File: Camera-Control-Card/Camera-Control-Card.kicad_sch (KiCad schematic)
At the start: 2 parts, among them J2 Conn_01x10, U3 74AHC125

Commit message: updates
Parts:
- removed U3: 74AHC125, Package_SO:TSSOP-14_4.4x5mm_P0.65mm, symbol 74xx:74AHCT125
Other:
- added sheet Buffer_3V3 (Buffer_3V3.kicad_sch)

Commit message: test
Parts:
- removed J2: Conn_01x10, Connector_PinHeader_2.54mm:PinHeader_2x05_P2.54mm_Vertical, symbol Connector_Generic:Conn_01x10
- added J1, J2, J3, J4, J5: Conn_Coaxial, Connector_Coaxial:SMA_Molex_73251-1153_EdgeMount_Horizontal, symbol Connector:Conn_Coaxial
- added J6: Conn_02x05_Counter_Clockwise, symbol Connector_Generic:Conn_02x05_Counter_Clockwise
- added J8: SFV24R-1STE1HLF, Footprints:AMPHENOL_SFV24R-1STE1HLF, symbol Symbols:SFV24R-1STE1HLF
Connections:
- net +3V3: now also J6.1 (Pin_1)
- net Buffer_3V3/OUT_0: now also J1.1 (In)
- net Buffer_3V3/OUT_1: now also J2.1 (In)
- net Buffer_3V3/OUT_2: now also J3.1 (In)
- net Buffer_3V3/OUT_3: now also J4.1 (In)
- net GND: now also J1.2 (Ext), J2.2 (Ext), J3.2 (Ext), J4.2 (Ext), J5.2 (Ext), J6.4 (Pin_4), J6.5 (Pin_5), J8.10, J8.12, J8.14, J8.16, J8.18, J8.2, J8.20, J8.22, J8.24, J8.4, J8.6, J8.8
- new net Buffer_3V3/OUT_4: J5.1 (In)
- new net DONE: J6.6 (Pin_6)
- new net INIT_N: J6.3 (Pin_3)
- new net PROGRAMN: J6.7 (Pin_7)
- new net TCK: J6.8 (Pin_8)
- new net TDI: J6.10 (Pin_10)
- new net TDO: J6.9 (Pin_9)
- new net TMS: J6.2 (Pin_2)
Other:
- sheet Buffer_3V3 ports: added IN_4, OE_4, OUT_4; removed none

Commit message: Updates
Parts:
- J2: renamed from J6; footprint (none) -> Footprints:AMPHENOL_78207-110HLF
- renumbered J8 to J1, J1 to J3, J2 to J4, J3 to J5, J4 to J6, J5 to J7
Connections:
- net PROGRAMN: now also J2.2 (Pin_2); no longer J2.7 (Pin_7)
- net TCK: now also J2.9 (Pin_9); no longer J2.8 (Pin_8)
- net TDI: now also J2.8 (Pin_8); no longer J2.10 (Pin_10)
- net TDO: now also J2.7 (Pin_7); no longer J2.9 (Pin_9)
- net TMS: now also J2.10 (Pin_10); no longer J2.2 (Pin_2)
- net FPGA/PT35B: now reaches J1.1
- net FPGA/PT28A: now reaches J1.11
- net FPGA/PT25B: now reaches J1.13
- net FPGA/PT25A: now reaches J1.15
- net FPGA/PT22D: now reaches J1.17
- net FPGA/PT22C: now reaches J1.19
- net FPGA/PT18B: now reaches J1.21
- net FPGA/PT18A: now reaches J1.23
- net FPGA/PT35A: now reaches J1.3
- net FPGA/PT33B: now reaches J1.5
- net FPGA/PT33A: now reaches J1.7
- net FPGA/PT28B: now reaches J1.9
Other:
- added sheet USB (USB.kicad_sch)
- sheet FPGA ports: added PT18A, PT18B, PT22C, PT22D, PT25A, PT25B, PT28A, PT28B, PT33A, PT33B, PT35A, PT35B; removed none

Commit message: Camera Control Card layout
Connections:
- net +3V3: now also J2.4 (Pin_4); no longer J2.1 (Pin_1)
- net DONE: now also J2.3 (Pin_3); no longer J2.6 (Pin_6)
- net GND: now also J2.1 (Pin_1), J2.2 (Pin_2); no longer J2.4 (Pin_4), J2.5 (Pin_5)
- net INIT_N: now also J2.6 (Pin_6); no longer J2.3 (Pin_3)
- net PROGRAMN: now also J2.5 (Pin_5); no longer J2.2 (Pin_2)
- no-connect marks 5 -> 2
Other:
- sheet FPGA ports: added MISO_1_BUF, MISO_2_BUF, MOSI_1, MOSI_2, PB26A, PB26B, SCK_1, SCK_2; removed MISO, MOSI, SCK
- sheet USB ports: added +3V3, GND, RXD, TXD; removed none
- moved on the sheet: J1, J2, J3, J4, J5, J6, J7

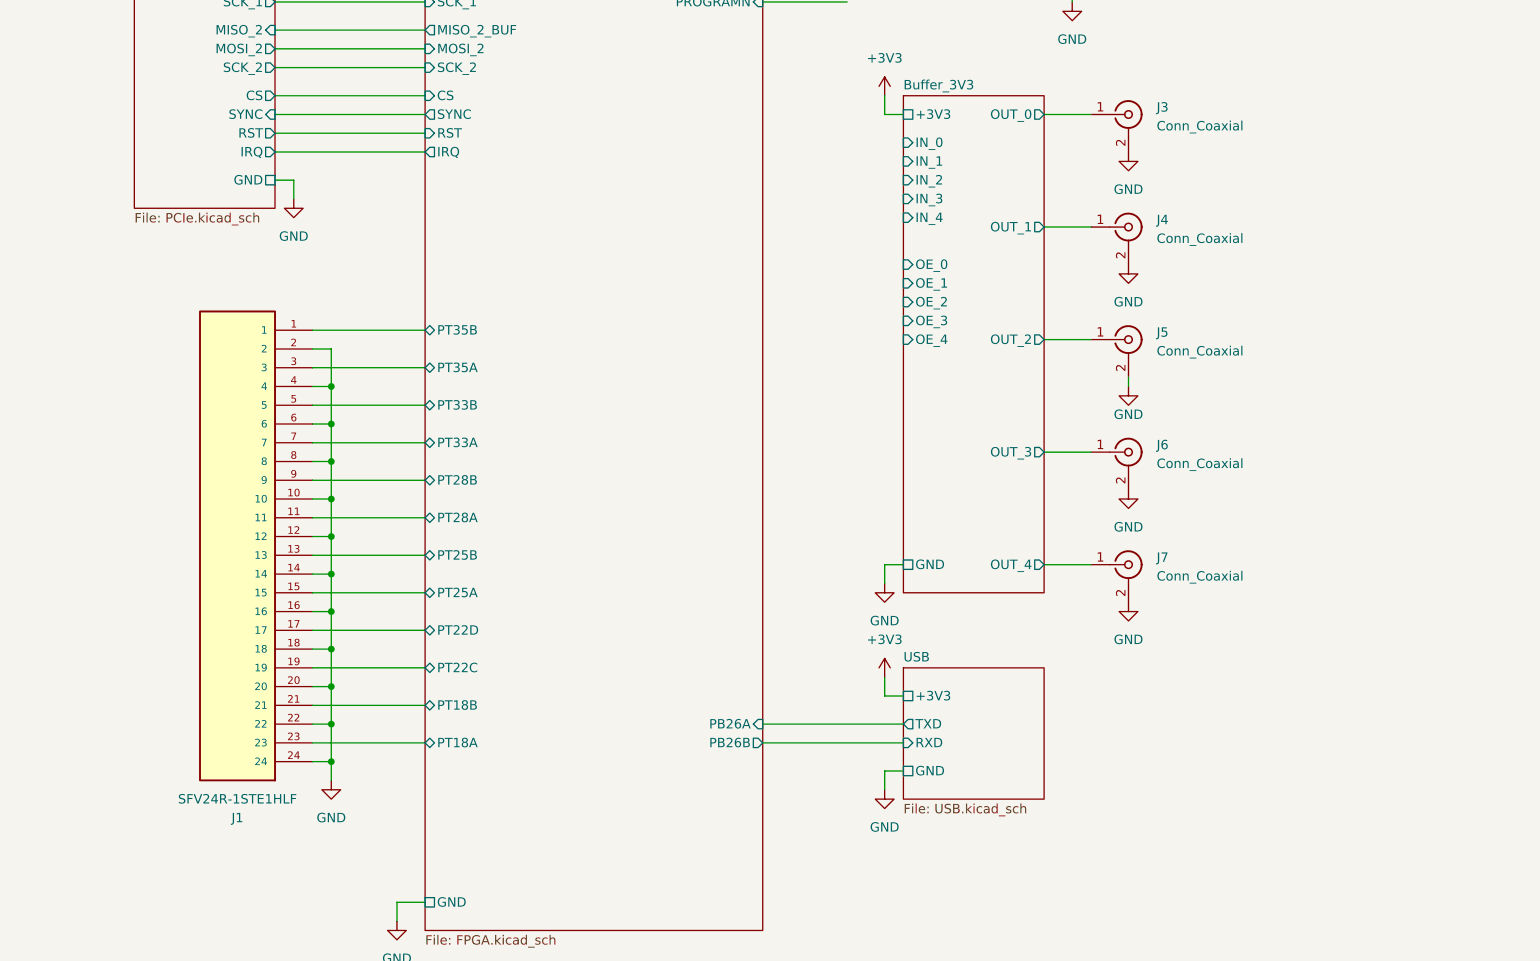
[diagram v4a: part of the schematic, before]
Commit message: Layout completed for camera control card
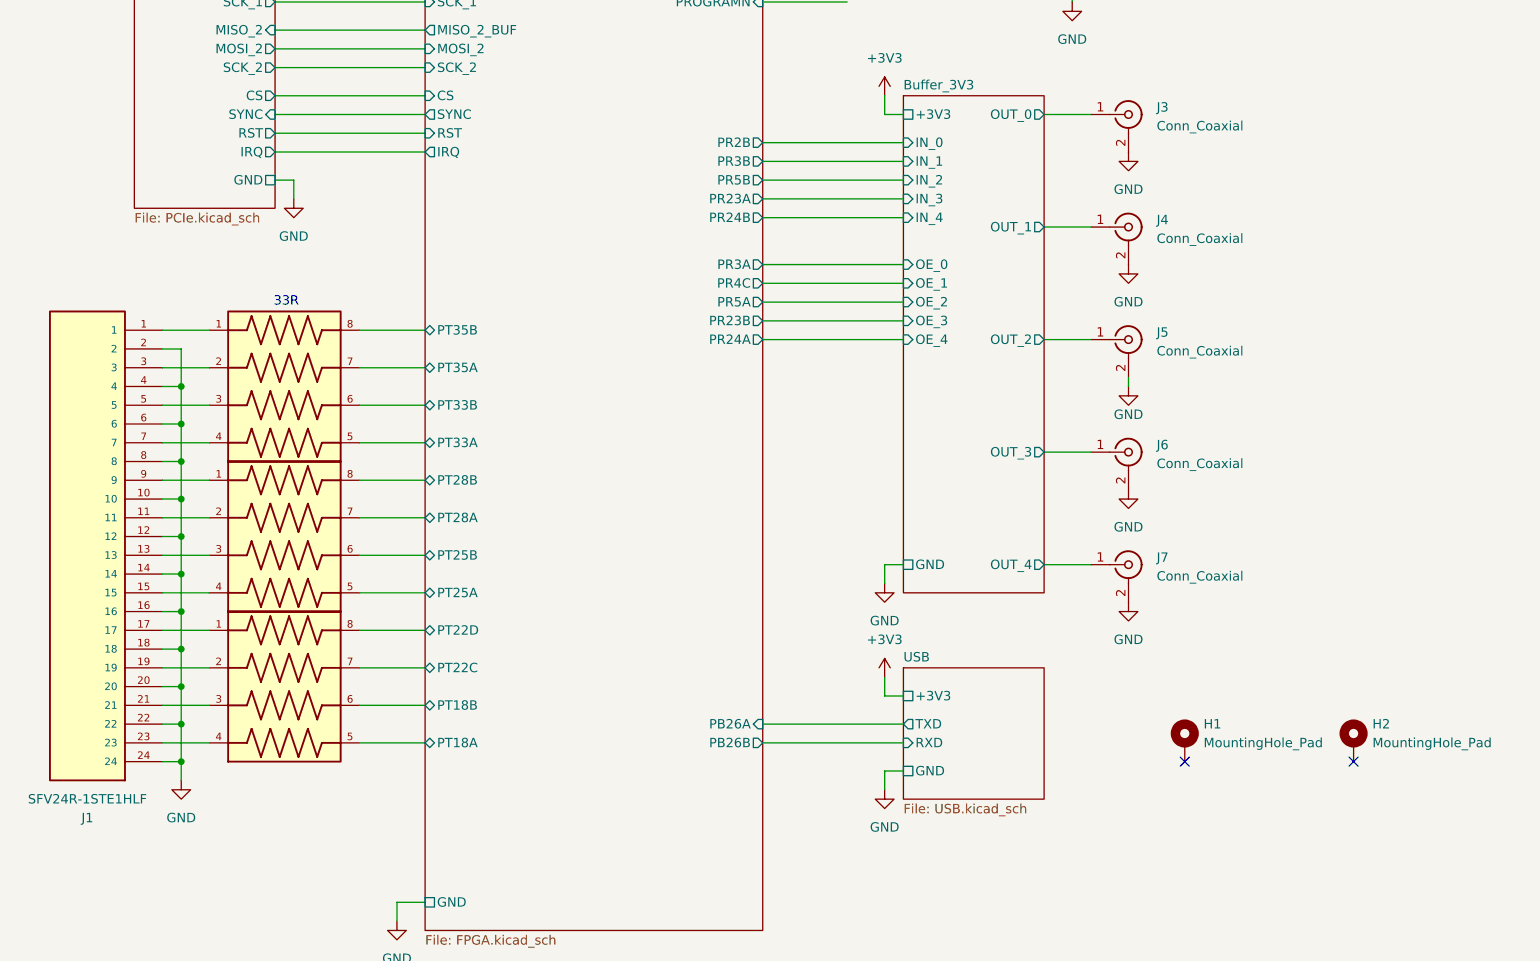
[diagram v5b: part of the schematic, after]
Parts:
- added H1, H2: MountingHole_Pad, MountingHole:MountingHole_2.2mm_M2_DIN965_Pad_TopBottom, symbol Mechanical:MountingHole_Pad
- added RN1, RN2, RN3: EXB-38V330JV, Footprints:RESCAXS80P320X160X60-8N, symbol Symbols:EXB-38V330JV
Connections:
- net FPGA/PT18A: now also RN3.5; no longer J1.23
- net FPGA/PT18B: now also RN3.6; no longer J1.21
- net FPGA/PT22C: now also RN3.7; no longer J1.19
- net FPGA/PT22D: now also RN3.8; no longer J1.17
- net FPGA/PT25A: now also RN2.5; no longer J1.15
- net FPGA/PT25B: now also RN2.6; no longer J1.13
- net FPGA/PT28A: now also RN2.7; no longer J1.11
- net FPGA/PT28B: now also RN2.8; no longer J1.9
- net FPGA/PT33A: now also RN1.5; no longer J1.7
- net FPGA/PT33B: now also RN1.6; no longer J1.5
- net FPGA/PT35A: now also RN1.7; no longer J1.3
- net FPGA/PT35B: now also RN1.8; no longer J1.1
- new net: J1.17, RN3.1
- new net: J1.19, RN3.2
- new net: J1.21, RN3.3
- new net: J1.23, RN3.4
- new net: J1.9, RN2.1
- new net: J1.11, RN2.2
- new net: J1.13, RN2.3
- new net: J1.15, RN2.4
- new net: J1.1, RN1.1
- new net: J1.3, RN1.2
- new net: J1.5, RN1.3
- new net: J1.7, RN1.4
- no-connect marks 2 -> 4
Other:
- sheet FPGA ports: added PR23A, PR23B, PR24A, PR24B, PR2B, PR3A, PR3B, PR4C, PR5A, PR5B; removed none
- note added: "33R"
- moved on the sheet: J1
